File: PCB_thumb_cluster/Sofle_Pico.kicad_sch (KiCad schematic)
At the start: 11 parts, among them J3 Conn_02x03, SW1 SW_PUSH, SW2 SW_PUSH, SW3 SW_PUSH, SW4 SW_PUSH, SW5 SW_PUSH

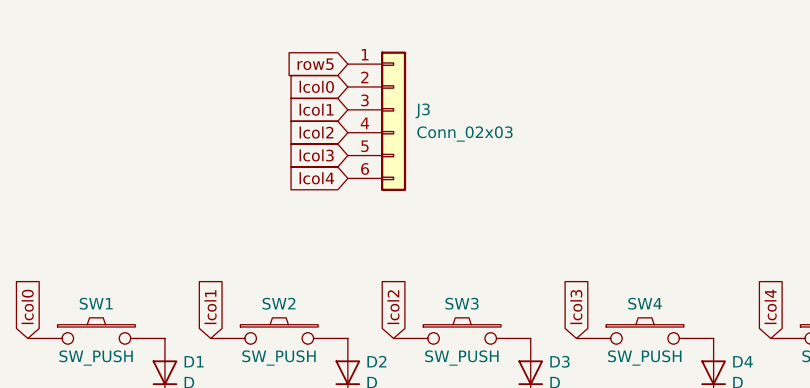
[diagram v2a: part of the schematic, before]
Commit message: thumb cluster connection uses idc
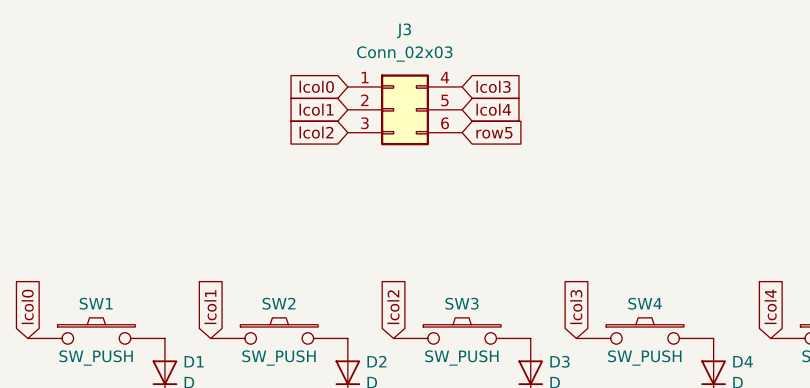
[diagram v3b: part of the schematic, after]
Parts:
- J3: footprint Connector_PinHeader_2.54mm:PinHeader_2x03_P2.54mm_Vertical -> Connector_PinHeader_2.00mm:PinHeader_2x03_P2.00mm_Vertical; symbol Connector_Generic:Conn_01x06 -> Connector_Generic:Conn_02x03_Top_Bottom
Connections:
- net lcol0: now also J3.1 (Pin_1); no longer J3.2 (Pin_2)
- net lcol1: now also J3.2 (Pin_2); no longer J3.3 (Pin_3)
- net lcol2: now also J3.3 (Pin_3); no longer J3.4 (Pin_4)
- net lcol3: now also J3.4 (Pin_4); no longer J3.5 (Pin_5)
- net lcol4: now also J3.5 (Pin_5); no longer J3.6 (Pin_6)
- net row5: now also J3.6 (Pin_6); no longer J3.1 (Pin_1)
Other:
- moved on the sheet: J3
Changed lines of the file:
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@@
-		)
-	)
-	(global_label "row5"
-		(shape input)
-		(at 66.04 44.45 180)
-		(effects
-			(font
-				(size 1.27 1.27)
-			)
-			(justify right)
-		)
-		(property "Intersheetrefs" "${INTERSHEET_REFS}"
-			(at 66.04 44.45 0)
-			(effects
-				(font
-					(size 1.27 1.27)
-				)
-				(hide yes)
-			)
 		)
 	)
@@
 		)
 	)
+	(global_label "lcol0"
+		(shape input)
+		(at 66.04 46.99 180)
+		(effects
+			(font
+				(size 1.27 1.27)
+			)
+			(justify right)
+		)
+		(property "Intersheetrefs" "${INTERSHEET_REFS}"
+			(at 66.04 46.99 90)
+			(effects
+				(font
+					(size 1.27 1.27)
+				)
+				(hide yes)
+			)
+		)
+	)
 	(global_label "row5"
 		(shape input)
@@
 		)
 	)
+	(global_label "lcol4"
+		(shape input)
+		(at 78.74 49.53 0)
+		(effects
+			(font
+				(size 1.27 1.27)
+			)
+			(justify left)
+		)
+		(property "Intersheetrefs" "${INTERSHEET_REFS}"
+			(at 78.74 49.53 90)
+			(effects
+				(font
+					(size 1.27 1.27)
+				)
+				(hide yes)
+			)
+		)
+	)
+	(global_label "lcol0"
+		(shape input)
+		(at 30.48 74.93 90)
+		(effects
+			(font
+				(size 1.27 1.27)
+			)
+			(justify left)
+		)
+		(property "Intersheetrefs" "${INTERSHEET_REFS}"
+			(at 30.48 74.93 0)
+			(effects
+				(font
+					(size 1.27 1.27)
+				)
+				(hide yes)
+			)
+		)
+	)
+	(global_label "lcol3"
+		(shape input)
+		(at 78.74 46.99 0)
+		(effects
+			(font
+				(size 1.27 1.27)
+			)
+			(justify left)
+		)
+		(property "Intersheetrefs" "${INTERSHEET_REFS}"
+			(at 78.74 46.99 90)
+			(effects
+				(font
+					(size 1.27 1.27)
+				)
+				(hide yes)
+			)
+		)
+	)
+	(global_label "lcol2"
+		(shape input)
+		(at 66.04 52.07 180)
+		(effects
+			(font
+				(size 1.27 1.27)
+			)
+			(justify right)
+		)
+		(property "Intersheetrefs" "${INTERSHEET_REFS}"
+			(at 66.04 52.07 90)
+			(effects
+				(font
+					(size 1.27 1.27)
+				)
+				(hide yes)
+			)
+		)
+	)
+	(global_label "lcol3"
+		(shape input)
+		(at 91.44 74.93 90)
+		(effects
+			(font
+				(size 1.27 1.27)
+			)
+			(justify left)
+		)
+		(property "Intersheetrefs" "${INTERSHEET_REFS}"
+			(at 91.44 74.93 0)
+			(effects
+				(font
+					(size 1.27 1.27)
+				)
+				(hide yes)
+			)
+		)
+	)
 	(global_label "lcol1"
 		(shape input)
@@
 		)
 	)
-	(global_label "lcol3"
-		(shape input)
-		(at 66.04 54.61 180)
-		(effects
-			(font
-				(size 1.27 1.27)
-			)
-			(justify right)
-		)
-		(property "Intersheetrefs" "${INTERSHEET_REFS}"
-			(at 66.04 54.61 90)
-			(effects
-				(font
-					(size 1.27 1.27)
-				)
-				(hide yes)
-			)
-		)
-	)
-	(global_label "lcol4"
-		(shape input)
-		(at 66.04 57.15 180)
-		(effects
-			(font
-				(size 1.27 1.27)
-			)
-			(justify right)
-		)
-		(property "Intersheetrefs" "${INTERSHEET_REFS}"
-			(at 66.04 57.15 90)
-			(effects
-				(font
-					(size 1.27 1.27)
-				)
-				(hide yes)
-			)
-		)
-	)
-	(global_label "lcol0"
-		(shape input)
-		(at 30.48 74.93 90)
-		(effects
-			(font
-				(size 1.27 1.27)
-			)
-			(justify left)
-		)
-		(property "Intersheetrefs" "${INTERSHEET_REFS}"
-			(at 30.48 74.93 0)
-			(effects
-				(font
-					(size 1.27 1.27)
-				)
-				(hide yes)
-			)
-		)
-	)
-	(global_label "lcol2"
-		(shape input)
-		(at 66.04 52.07 180)
-		(effects
-			(font
-				(size 1.27 1.27)
-			)
-			(justify right)
-		)
-		(property "Intersheetrefs" "${INTERSHEET_REFS}"
-			(at 66.04 52.07 90)
-			(effects
-				(font
-					(size 1.27 1.27)
-				)
-				(hide yes)
-			)
-		)
-	)
-	(global_label "lcol0"
-		(shape input)
-		(at 66.04 46.99 180)
-		(effects
-			(font
-				(size 1.27 1.27)
-			)
-			(justify right)
-		)
-		(property "Intersheetrefs" "${INTERSHEET_REFS}"
-			(at 66.04 46.99 90)
-			(effects
-				(font
-					(size 1.27 1.27)
-				)
-				(hide yes)
-			)
-		)
-	)
-	(global_label "lcol3"
-		(shape input)
-		(at 91.44 74.93 90)
-		(effects
-			(font
-				(size 1.27 1.27)
-			)
-			(justify left)
-		)
-		(property "Intersheetrefs" "${INTERSHEET_REFS}"
-			(at 91.44 74.93 0)
-			(effects
-				(font
-					(size 1.27 1.27)
-				)
-				(hide yes)
-			)
-		)
-	)
 	(global_label "lcol4"
 		(shape input)
@@
 		)
 	)
+	(global_label "row5"
+		(shape input)
+		(at 78.74 52.07 0)
+		(effects
+			(font
+				(size 1.27 1.27)
+			)
+			(justify left)
+		)
+		(property "Intersheetrefs" "${INTERSHEET_REFS}"
+			(at 78.74 52.07 0)
+			(effects
+				(font
+					(size 1.27 1.27)
+				)
+				(hide yes)
+			)
+		)
+	)
 	(symbol
 		(lib_id "Sofle_Pico:SW_PUSH")
@@
 	)
 	(symbol
-		(lib_id "Connector_Generic:Conn_01x06")
+		(lib_id "Connector_Generic:Conn_02x03_Top_Bottom")
 		(at 71.12 49.53 0)
 		(unit 1)
@@
 		(fields_autoplaced yes)
 		(property "Reference" "J3"
-			(at 73.66 49.5299 0)
-			(effects
-				(font
-					(size 1.27 1.27)
-				)
-				(justify left)
+			(at 72.39 40.64 0)
+			(effects
+				(font
+					(size 1.27 1.27)
+				)
 			)
 		)
 		(property "Value" "Conn_02x03"
-			(at 73.66 52.0699 0)
-			(effects
-				(font
-					(size 1.27 1.27)
-				)
-				(justify left)
-			)
-		)
-		(property "Footprint" "Connector_PinHeader_2.54mm:PinHeader_2x03_P2.54mm_Vertical"
+			(at 72.39 43.18 0)
+			(effects
+				(font
+					(size 1.27 1.27)
+				)
+			)
+		)
+		(property "Footprint" "Connector_PinHeader_2.00mm:PinHeader_2x03_P2.00mm_Vertical"
 			(at 71.12 49.53 0)
 			(effects
@@
 			)
 		)
-		(property "Description" "Generic connector, single row, 01x06, script generated (kicad-library-utils/schlib/autogen/connector/)"
+		(property "Description" "Generic connector, double row, 02x03, top/bottom pin numbering scheme (row 1: 1...pins_per_row, row2: pins_per_row+1 ... num_pins), script generated (kicad-library-utils/schlib/autogen/connector/)"
 			(at 71.12 49.53 0)
 			(effects
